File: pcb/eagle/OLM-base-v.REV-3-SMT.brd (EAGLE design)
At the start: 100 x 74.9 mm, 96 parts, among them IC1 ENC28J60, IC3 MCP73871, IC4 ATMEGA32U4-AU, IC6 DS3231SN, U1 USD-SOCKETMICRO-SD-SOCKET-TAO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, U2 BMP085, U3 AM2302, X1 8MHz, X2A 25MHz

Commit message: fixed design
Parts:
- removed BATT: (no value), adafruit:JST-PH-2-SMT-RA
- added BATT3V7: (no value), adafruit:JST-PH-2-SMT-RA
- moved B1 108.9 mm to (3.81, 62.2), turned to 270 degrees
- moved BTN 85.3 mm to (87.6, 39.4), turned to 270 degrees
- moved RN1 62.0 mm to (30.5, 16.5)
- moved C9 22.5 mm to (39.4, 38.1)
- moved C12 8.98 mm to (81.3, 29.2)
- moved LUX1 7.62 mm to (96.5, 40.6)
- moved LUX2 7.62 mm to (96.5, 44.5), turned to 270 degrees
- moved X1 5.08 mm to (21.6, 35.6)
- moved HOBBY 5.08 mm to (3.81, 57.1)
- moved C8 3.81 mm to (24.1, 53.3)
- moved CON2 3.81 mm to (85.1, 71.1)
- moved SOLAR 3.81 mm to (3.81, 47.0)
- moved C4 3.59 mm to (87.6, 57.1)
- moved C6 2.54 mm to (30.5, 53.3)
- moved CON1 2.54 mm to (64.8, 71.1)
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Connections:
- net BATT: now also BATT3V7.1; no longer BATT.1
- net GND: now also BATT3V7.2; no longer BATT.2

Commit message: more pcb changes
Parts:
- removed BAT1: (no value), SparkFunNew:BATTCON_12MM_SMT
- removed BATT3V7: (no value), adafruit:JST-PH-2-SMT-RA
- removed CAP1: 10u, resistor:C0805
- removed CHRG/LBO: ORANGE, adafruit:CHIP-LED0805
- removed IC4: ATMEGA32U4-AU, adaprog:TQFP44
- removed IC6: DS3231SN, comfile:SO16W
- removed JP3: M10LOCK, SparkFun-Connectors:1X10_LOCK
- removed LDO3V3: MCP1703CB, linear:SOT23
- removed LUX1: TSL2561, microbuilder:TSL2561_FN@1
- removed LUX2: TCS34725, dwbLibrary:DFN-6
- removed RBS1: 2.32K, rcl:R0805
- removed U2: BMP085, microbuilder:BMP085
- removed X2A: 25MHz, SparkFun:CRYSTAL-SMD-10.5X4.8-2PIN
- added BATRTC: (no value), SparkFunNew:BATTCON_12MM_SMT
- added BATT3V1: (no value), adafruit:JST-PH-2-SMT-RA
- added C24: 10uF, adafruit:C0805
- added CHRG: ORANGE, adafruit:CHIP-LED0805
- added EXTL: 25MHz, SparkFun:CRYSTAL-SMD-10.5X4.8-2PIN
- added IC2: MCP73871, adafruit:QFN20_4MM
- added JP1: ICSP, pinhead:2X03
- added LDO3V1: MCP1703CB, linear:SOT23
- added LUXNIR: TSL2561, microbuilder:TSL2561_FN@1
- added LUXRGB: TCS34725, dwbLibrary:DFN-6
- added PRESS: BMP085, microbuilder:BMP085
- added R4: 1K, adafruit:R0805
- added RTC: DS3231SN, comfile:SO16W
- C1: value 0.1µ -> 10u
- C3: value 1uF -> 0.1µ; device adafruit:C0805 -> resistor:C0805
- C4: value 4700uF/10V -> 1uF; device adafruit:E5-13 -> adafruit:C0805
- C5: value 10uF/10V -> 4700uF/10V; device adafruit:C0805 -> adafruit:E5-13
- C6: value 10uF -> 10uF/10V
- C7: value .1uF -> 10uF
- C8: value 10uF -> .1uF
- IC3: value MCP73871 -> ATMEGA32U4-AU; device adafruit:QFN20_4MM -> adaprog:TQFP44
- JP2: value ICSP -> M10LOCK; device pinhead:2X03 -> SparkFun-Connectors:1X10_LOCK
- R1: value 22 -> 2.32K; device adafruit:R0805 -> rcl:R0805
- R17: value 2.2K -> 10K
- R19: value 10K -> 2.2K
- R3: value 1K -> 22
- moved R17 76.5 mm to (95.2, 6.35)
- moved C5 75.2 mm to (87.6, 57.1), turned to 270 degrees
- moved SW 68.9 mm to (16.0, 4.32), turned to 180 degrees
- moved R2 65.6 mm to (14.7, 35.6)
- moved EMBD 65.1 mm to (91.7, 77.5), turned to 180 degrees
- moved JP2 64.6 mm to (59.2, 78.2), turned to 0 degrees
- moved HOBBY 64.3 mm to (67.1, 68.8), turned to 0 degrees
- moved R21 63.8 mm to (82.5, 2.54), turned to 90 degrees
- moved C18 61.6 mm to (85.1, 34.3)
- moved C20 60.2 mm to (85.3, 38.6)
- moved C23 59.4 mm to (74.9, 10.2)
- moved THERM 59.1 mm to (28.7, 29.0), turned to 180 degrees
- moved C2 55.0 mm to (36.6, 13.2), turned to 180 degrees
- moved R3 54.7 mm to (14.2, 39.4)
- moved C17 54.0 mm to (73.4, 32.3), turned to 90 degrees
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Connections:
- net +3V3: now also IC3.42, IC3.6, LDO3V1.2, LUXNIR.VDD, LUXRGB.1, PRESS.P$3, PRESS.P$4, R17.1, R21.1, RTC.2; no longer IC4.42, IC4.6, IC6.2, LDO3V3.2, LUX1.VDD, LUX2.1, R16.1, R19.1, U2.P$3, U2.P$4
- net A0: now also IC3.36; no longer IC4.36
- net A1: now also IC3.37; no longer IC4.37
- net A2: now also IC3.38; no longer IC4.38
- net A3: now also IC3.39; no longer IC4.39
- net A4: now also IC3.40; no longer IC4.40
- net A5: now also IC3.41; no longer IC4.41
- net BATT: now also BATT3V1.1, IC2.P$14, IC2.P$15, IC2.P$16; no longer BATT3V7.1, IC3.P$14, IC3.P$15, IC3.P$16
- net D+: now also IC3.4, R2.2; no longer IC4.4, R1.2
- net D-: now also IC3.3, R3.2; no longer IC4.3, R2.2
- net D0/RX: now also IC3.20; no longer IC4.20
- net D1/TX: now also IC3.21; no longer IC4.21
- net D4/A6: now also IC3.25; no longer IC4.25
- net D5*: now also IC3.31; no longer IC4.31
- net D6*/A8: now also IC3.27, R19.1, R20.2; no longer IC4.27, R18.1, R19.2
- net D7/AIN0: now also IC3.1, R17.2; no longer IC4.1, R16.2
- net GND: now also BATRTC.P$1, BATT3V1.2, C1.2, C4.1, C5.-, C6.2, C8.1, IC2.P$10, IC2.P$11, IC2.P$21, IC3.15, IC3.23, IC3.33, IC3.35, IC3.43, IC3.5, JP1.6, JP2.1, LDO3V1.1, LUXNIR.VSS, LUXRGB.3, PRESS.P$1, R1.1, R16.1, RTC.10, RTC.11, RTC.12, RTC.13, RTC.5, RTC.6, RTC.7, RTC.8, RTC.9; no longer BAT1.P$1, BATT3V7.2, C1.1, C4.-, C5.2, C6.1, CAP1.2, IC3.P$10, IC3.P$11, IC3.P$21, IC4.15, IC4.23, IC4.33, IC4.35, IC4.43, IC4.5, IC6.10, IC6.11, IC6.12, IC6.13, IC6.5, IC6.6, IC6.7, IC6.8, IC6.9, JP2.6, JP3.1, LDO3V3.1, LUX1.VSS, LUX2.3, R21.1, RBS1.1, U2.P$1
- net IO10*/A11: now also IC3.30; no longer IC4.30
- net IO11*: now also IC3.12; no longer IC4.12
- net IO12*/A7: now also IC3.26, R18.1; no longer IC4.26, R17.1
- net IO13*: now also IC3.32; no longer IC4.32
- net IO8/A9: now also IC3.28, R16.2; no longer IC4.28, R21.2
- net IO9*/A10: now also IC3.29; no longer IC4.29
- net MISO: now also IC3.11, JP1.1; no longer IC4.11, JP2.1
- net MOSI: now also IC3.10, JP1.4; no longer IC4.10, JP2.4
- net N$1: now also BATRTC.P$2, RTC.14; no longer BAT1.P$2, IC6.14
- net N$10: now also C2.2; no longer C1.2
- net N$16: now also C1.1; no longer CAP1.1
- net N$17: now also R1.2; no longer RBS1.2
- net N$18: now also EXTL.P$2; no longer X2A.P$2
- net N$19: now also EXTL.P$1; no longer X2A.P$1
- net N$20: now also IC2.P$2; no longer IC3.P$2
- net N$21: now also IC2.P$6; no longer IC3.P$6
- net N$22: now also C4.2, C5.+, C6.1; no longer C3.2, C4.+, C5.1
- net N$29: now also CHRG.C, IC2.P$8; no longer CHRG/LBO.C, IC3.P$8
- net N$30: now also CHRG.A, R4.1; no longer CHRG/LBO.A, R3.1
- net N$33: now also IC2.P$12; no longer IC3.P$12
- net N$34: now also IC2.P$13; no longer IC3.P$13
- net N$35: now also IC2.P$1, IC2.P$20; no longer IC3.P$1, IC3.P$20
- net N$36: now also IC2.P$5; no longer IC3.P$5
- net N$41: now also R2.1; no longer R1.1
- net N$42: now also R3.1; no longer R2.1
- net N$44: now also LDO3V1.3; no longer LDO3V3.3
- net N$8: now also IC3.17; no longer IC4.17
- net N$9: now also IC3.16; no longer IC4.16
- net RGB-INT: now also LUXRGB.5; no longer LUX2.5
- net RST: now also IC3.13, JP1.5; no longer IC4.13, JP2.5
- net RTC-32KHZ: now also RTC.1; no longer IC6.1
- net RTC-INT: now also RTC.3; no longer IC6.3
- net RTC-RST: now also RTC.4; no longer IC6.4
- net RXLED/SS: now also IC3.8; no longer IC4.8
- net SCK: now also IC3.9, JP1.3, R21.2; no longer IC4.9, JP2.3, R20.2
- net SCL: now also IC3.18, JP2.9, LUXNIR.CLK, LUXRGB.2, PRESS.P$6, RTC.16; no longer IC4.18, IC6.16, JP3.9, LUX1.CLK, LUX2.2, U2.P$6
- net SDA: now also IC3.19, JP2.10, LUXNIR.DATA, LUXRGB.6, PRESS.P$7, RTC.15; no longer IC4.19, IC6.15, JP3.10, LUX1.DATA, LUX2.6, U2.P$7
- net TCT: now also C3.2; no longer C2.2
- net TXLED: now also IC3.22; no longer IC4.22
- net VCC: now also IC3.14, IC3.24, IC3.34, IC3.44; no longer IC4.14, IC4.24, IC4.34, IC4.44
- net VIN: now also C8.2, IC2.P$17, IC2.P$18, IC2.P$19, IC2.P$3, IC2.P$4, IC2.P$9, IC3.7, R19.2, R4.2; no longer C6.2, IC3.P$17, IC3.P$18, IC3.P$19, IC3.P$3, IC3.P$4, IC3.P$9, IC4.7, R17.2, R3.2
- net VIS-NIR-ADDR: now also LUXNIR.ADR; no longer LUX1.ADR
- net VIS-NIR-INT: now also LUXNIR.INT; no longer LUX1.INT
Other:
- board size 100 x 74.9 mm -> 100.1 x 73.2 mm

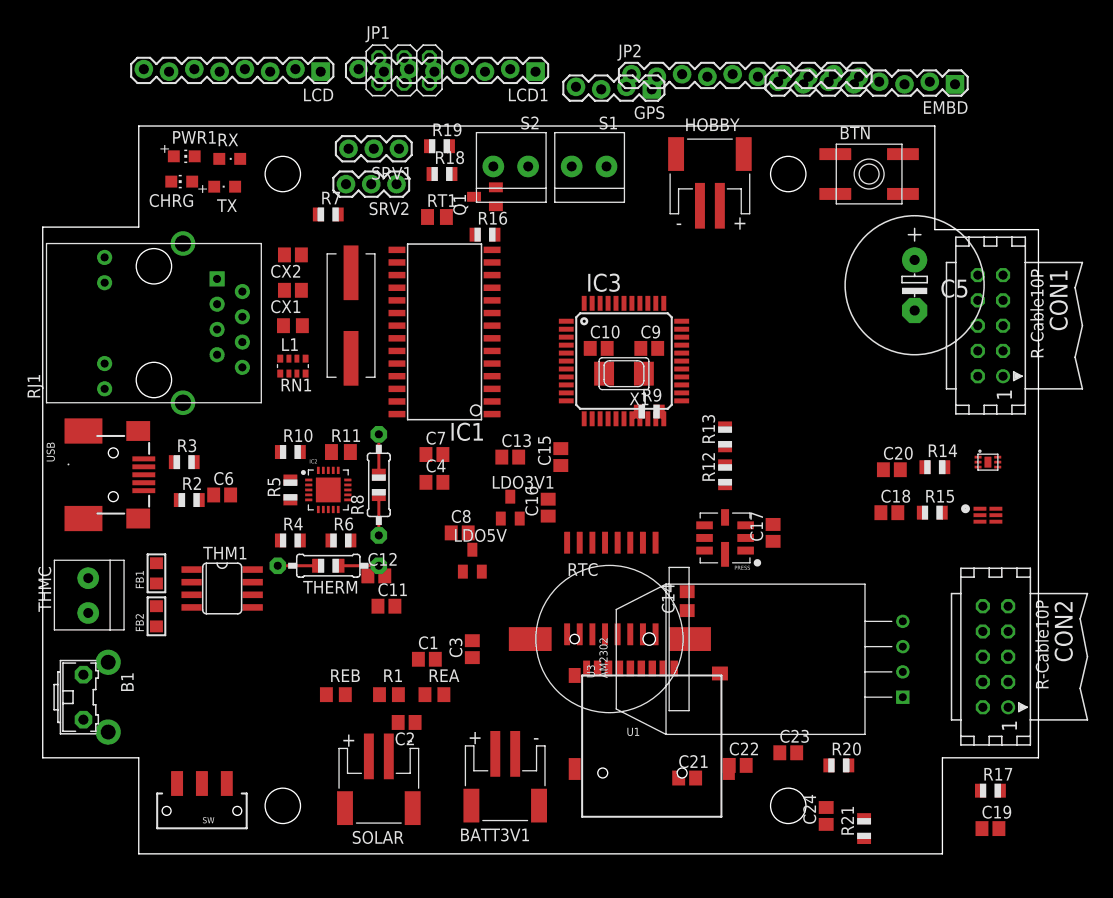
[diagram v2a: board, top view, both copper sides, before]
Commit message: updated layout
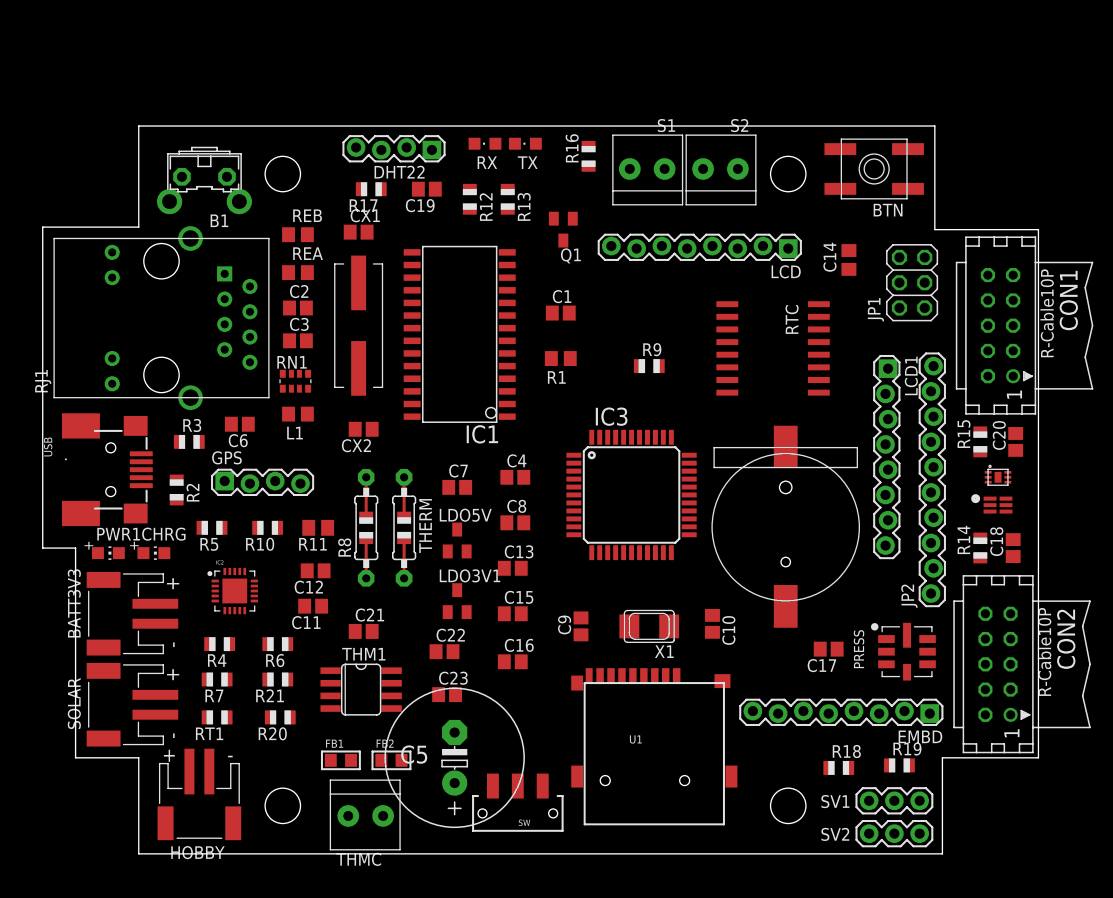
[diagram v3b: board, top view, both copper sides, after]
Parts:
- removed BATT3V1: (no value), adafruit:JST-PH-2-SMT-RA
- removed C24: 10uF, adafruit:C0805
- removed SRV1, SRV2: (no value), SparkFun:1X03
- removed U3: AM2302, sensor:AM2302
- added BATT3V3: (no value), adafruit:JST-PH-2-SMT-RA
- added DHT22: (no value), SparkFun-Connectors:1X04_LOCK
- added SV1, SV2: (no value), SparkFun:1X03
- RT1: device adafruit:M0805 -> adafruit:R0805
- moved R17 86.8 mm to (33.0, 66.8), turned to 180 degrees
- moved C19 85.7 mm to (38.6, 66.8), turned to 180 degrees
- moved HOBBY 82.2 mm to (15.7, 4.57), turned to 180 degrees
- moved R19 77.5 mm to (86.1, 8.89)
- moved R18 71.8 mm to (80.0, 8.64)
- moved C5 66.3 mm to (41.4, 9.65), turned to 90 degrees
- moved EMBD 63.3 mm to (89.2, 14.2)
- moved R21 60.8 mm to (23.6, 17.5), turned to 180 degrees
- moved JP2 60.2 mm to (89.4, 26.2), turned to 90 degrees
- moved GPS 58.4 mm to (18.3, 37.3), turned to 0 degrees
- moved R20 56.3 mm to (23.9, 13.7), turned to 180 degrees
- moved JP1 55.3 mm to (87.4, 57.4), turned to 90 degrees
- moved RT1 54.9 mm to (17.5, 13.7), turned to 180 degrees
- moved B1 52.2 mm to (16.3, 66.8), turned to 180 degrees
- moved LCD 50.2 mm to (74.9, 61.0)
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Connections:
- net +3V3: now also DHT22.1; no longer U3.P$1
- net BATT: now also BATT3V3.1; no longer BATT3V1.1
- net D6*/A8: now also SV2.3; no longer SRV2.3
- net D7/AIN0: now also DHT22.2; no longer U3.P$2
- net GND: now also BATT3V3.2, DHT22.4, RT1.2, SV1.1, SV2.1; no longer BATT3V1.2, RT1.1, SRV1.1, SRV2.1, U3.P$4
- net IO12*/A7: now also SV1.3; no longer SRV1.3
- net N$37: now also RT1.1; no longer RT1.2
- net VIN: now also SV1.2, SV2.2; no longer SRV1.2, SRV2.2
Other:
- outline, holes or cut-outs redrawn

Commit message: added some schematics
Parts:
- moved L1 1.02 mm to (25.7, 43.2), turned to 0 degrees
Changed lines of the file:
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@@
 <layer number="17" name="Pads" color="2" fill="1" visible="yes" active="yes"/>
 <layer number="18" name="Vias" color="2" fill="1" visible="yes" active="yes"/>
-<layer number="19" name="Unrouted" color="6" fill="1" visible="yes" active="yes"/>
+<layer number="19" name="Unrouted" color="6" fill="1" visible="no" active="yes"/>
 <layer number="20" name="Dimension" color="15" fill="1" visible="yes" active="yes"/>
 <layer number="21" name="tPlace" color="7" fill="1" visible="yes" active="yes"/>
@@
 <element name="EMBD" library="SparkFun-Connectors" package="1X08_LOCK" value="" x="89.154" y="14.224" rot="R180"/>
 <element name="U1" library="SparkFunNew" package="MICRO-SD-SOCKET-TAOBAO" value="USD-SOCKETMICRO-SD-SOCKET-TAOBAO" x="61.468" y="7.366"/>
-<element name="L1" library="rcl" package="R0805" value="Bead" x="25.654" y="44.196" rot="R180"/>
+<element name="L1" library="rcl" package="R0805" value="Bead" x="25.654" y="43.18"/>
 <element name="R1" library="rcl" package="R0805" value="2.32K" x="52.07" y="49.784" rot="R180"/>
 <element name="C3" library="resistor" package="C0805" value="0.1µ" x="25.654" y="51.562"/>
@@
 <wire x1="63.182" y1="41.868" x2="64.982" y2="32.868" width="0" layer="19" extent="1-1"/>
 <wire x1="55.182" y1="41.868" x2="63.182" y2="41.868" width="0" layer="19" extent="1-1"/>
-<wire x1="24.704" y1="44.196" x2="55.182" y2="41.868" width="0" layer="19" extent="1-1"/>
+<wire x1="26.604" y1="43.18" x2="55.182" y2="41.868" width="0" layer="19" extent="1-1"/>
 </signal>
 <signal name="N$11">
@@
 <wire x1="24.125" y1="48.248" x2="25" y2="48.248" width="0" layer="19" extent="1-1"/>
 <wire x1="26.504" y1="51.562" x2="24.125" y2="48.248" width="0" layer="19" extent="1-1"/>
-<wire x1="26.604" y1="44.196" x2="26.504" y2="51.562" width="0" layer="19" extent="1-1"/>
-<wire x1="20.828" y1="54.483" x2="26.604" y2="44.196" width="0" layer="19" extent="1-1"/>
+<wire x1="24.704" y1="43.18" x2="26.504" y2="51.562" width="0" layer="19" extent="1-1"/>
+<wire x1="20.828" y1="54.483" x2="24.704" y2="43.18" width="0" layer="19" extent="1-1"/>
 </signal>
 <signal name="TD+">
